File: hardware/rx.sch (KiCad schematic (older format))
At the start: 19 parts, among them P1 SMA, U11 SKY65404, U9 TRF37A73

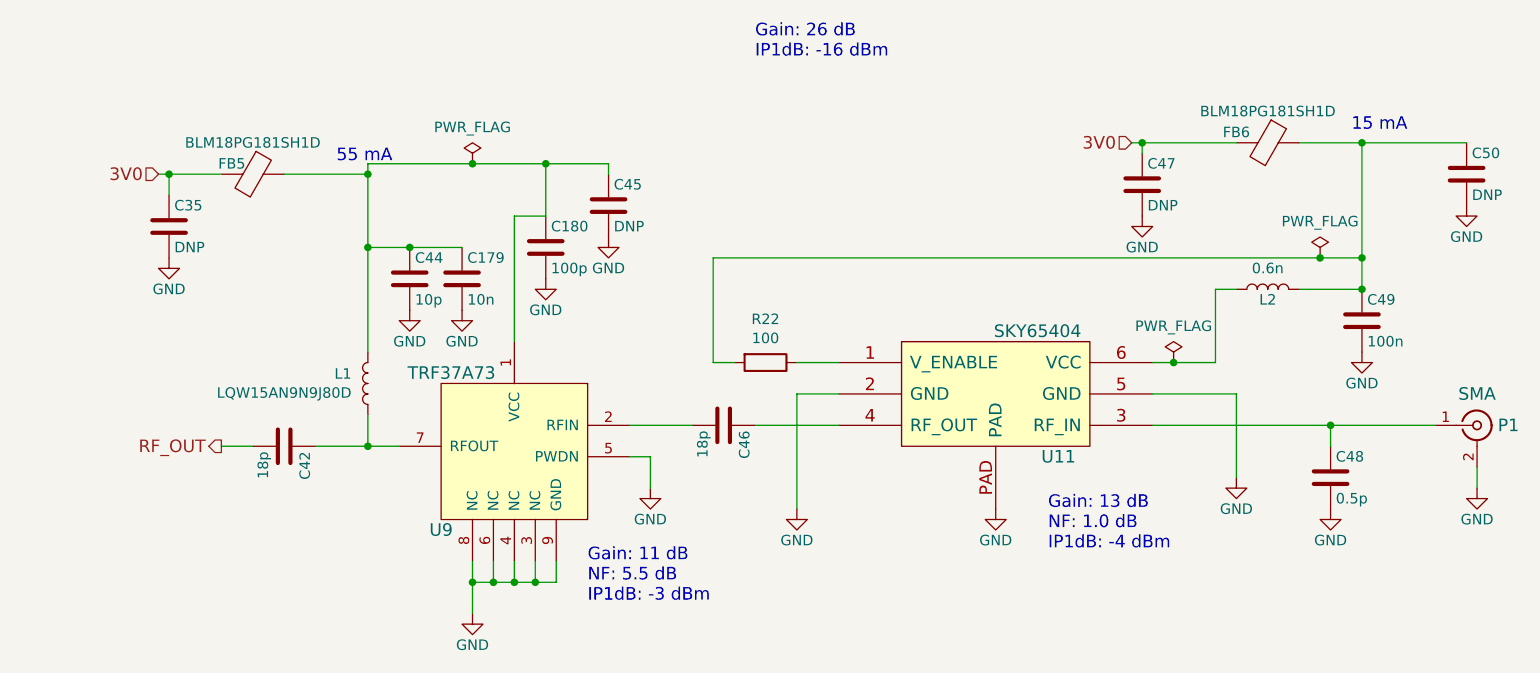
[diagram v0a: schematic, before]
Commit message: Improved tx sheet and corresponding documentation.
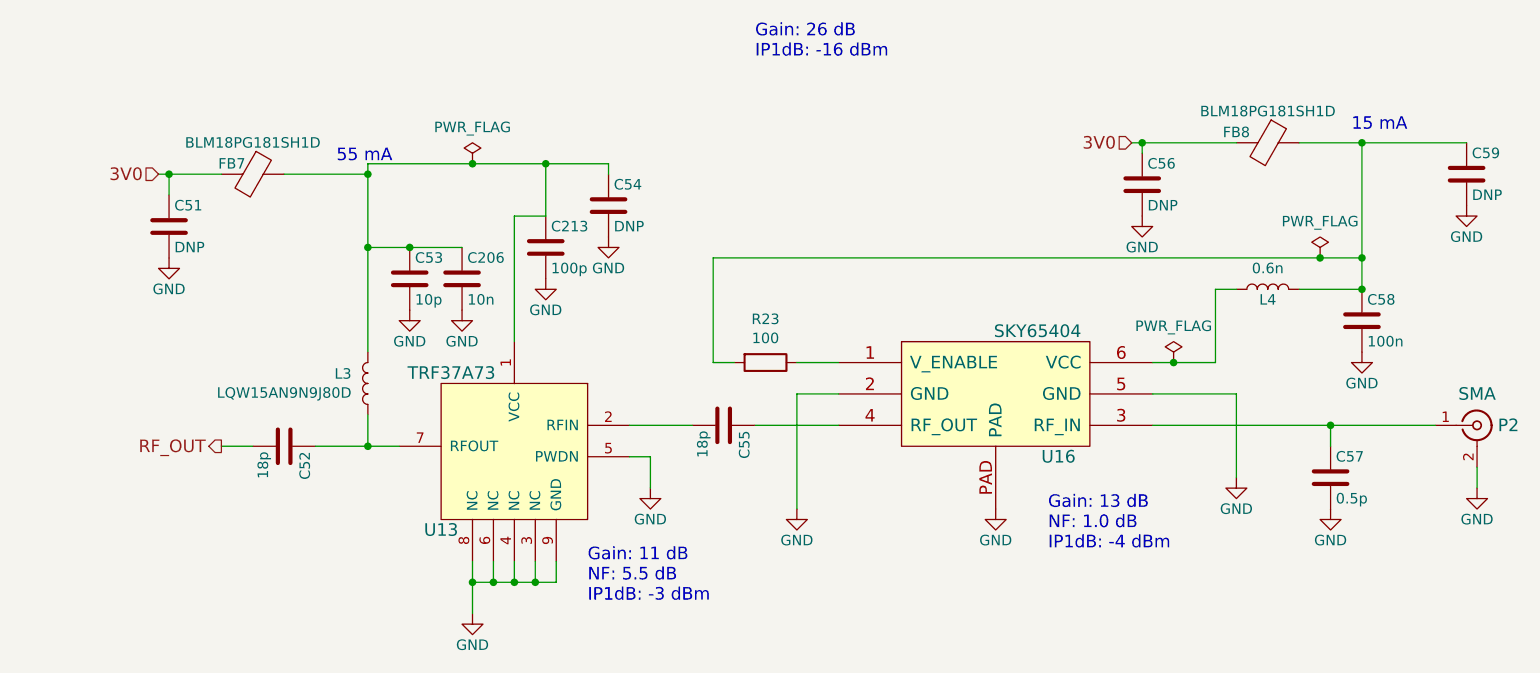
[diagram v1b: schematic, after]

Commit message: Improved documentation and parts of the schematic.
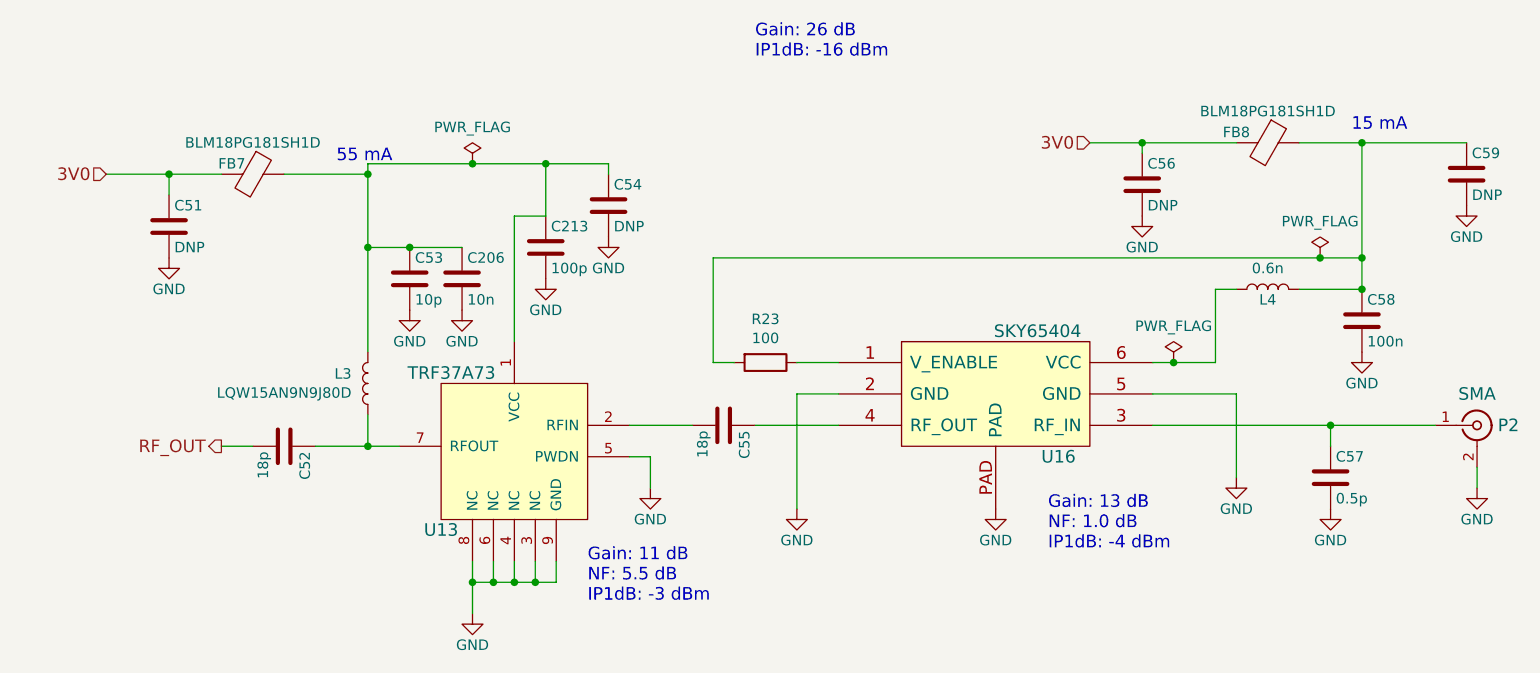
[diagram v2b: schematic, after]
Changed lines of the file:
@@
 $Descr A4 11693 8268
 encoding utf-8
-Sheet 6 10
+Sheet 7 10
 Title ""
 Date ""
@@
 Wire Wire Line
 	8600 2600 8600 3150
-Text HLabel 2850 2750 0    60   Input ~ 0
+Text HLabel 2600 2750 0    60   Input ~ 0
 3V0
-Text HLabel 7500 2600 0    60   Input ~ 0
+Text HLabel 7300 2600 0    60   Input ~ 0
 3V0
 Text HLabel 3150 4050 0    60   Output ~ 0
@@
 $EndComp
 Wire Wire Line
-	2850 2750 2900 2750
+	2600 2750 2900 2750
 $Comp
 L Device:C C54
@@
 $EndComp
 Wire Wire Line
-	7500 2600 7550 2600
+	7300 2600 7550 2600
 $Comp
 L Device:C C50

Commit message: Changed components to official libs.
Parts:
- added C51: 100n, Capacitor_SMD:C_0402_1005Metric, symbol Device:C
- C35, C47, C50: value DNP -> 100n; footprint Capacitor_SMD:C_0603_1608Metric -> Capacitor_SMD:C_0402_1005Metric; MFN (none) -> CL05B104KO5NNNC
- U11: footprint fmcw:XFDFN-6 -> Package_DFN_QFN:Skyworks_DFN-6-1EP_1.5x1.5mm_P0.5mm_EP0.7x1.2mm; symbol fmcw-rescue:SKY65404-fmcw3-rescue -> RF_Amplifier:SKY65404
- U9: footprint fmcw:DFN-8-1EP_2x2mm_Pitch0.5mm -> Package_SON:WSON-8-1EP_2x2mm_P0.5mm_EP0.9x1.6mm; symbol fmcw-rescue:TRF37A75-fmcw3-rescue -> RF_Amplifier:TRF37A73
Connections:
- net 3V0: now also C51.1; no longer C47.1
- net GND: now also U11.7 (EP), C51.2; no longer U11.PAD, U9.3 (NC), U9.4 (NC), U9.6 (NC), U9.8 (NC)
- net at C179.1, C180.1, C44.1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: now also C47.1
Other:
- moved on the sheet: C42, C48, C49, FB5, FB6, L1, L2, R22

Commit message: Finished design, began routing.
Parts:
- renumbered C35 to C145, C47 to C146, C42 to C147, C44 to C148, C179 to C149, C180 to C150, C46 to C152, C49 to C153, C48 to C154, C50 to C155, C51 to C156, C54 to C163, FB7 to FB13, FB8 to FB14, P1 to J4, R22 to R49, U9 to U22, U11 to U23

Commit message: Completed clock placement and routing.
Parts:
- removed C146, C155: 100n, Capacitor_SMD:C_0402_1005Metric, symbol Device:C

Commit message: Better MFNs for RF DC blocking caps.
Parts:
- C147, C152: MFN CL05C180GB5NCNC -> 500R07S180GV4T
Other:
- moved on the sheet: C163
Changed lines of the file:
@@
 $Descr A4 11693 8268
 encoding utf-8
-Sheet 6 10
+Sheet 7 10
 Title ""
 Date ""
@@
 F 2 "Capacitor_SMD:C_0402_1005Metric" H 5588 3800 30  0001 C CNN
 F 3 "" H 5550 3950 60  0000 C CNN
-F 4 "CL05C180GB5NCNC" H 0   0   50  0001 C CNN "MFN"
+F 4 "500R07S180GV4T" H 0   0   50  0001 C CNN "MFN"
 	1    5550 3950
 	0    1    1    0
@@
 F 2 "Capacitor_SMD:C_0402_1005Metric" H 3488 3800 30  0001 C CNN
 F 3 "" H 3450 3950 60  0000 C CNN
-F 4 "CL05C180GB5NCNC" H 0   -100 50  0001 C CNN "MFN"
+F 4 "500R07S180GV4T" H 0   -100 50  0001 C CNN "MFN"
 	1    3450 3950
 	0    1    1    0
@@
 L Device:C C163
 U 1 1 59751D28
-P 5000 2900
+P 5150 2900
 AR Path="/593D90BA/59751D28" Ref="C163"  Part="1"
 AR Path="/59396B97/59751D28" Ref="C151"  Part="1"
-F 0 "C163" H 5025 3000 50  0000 L CNN
-F 1 "DNP" H 5025 2800 50  0000 L CNN
-F 2 "Capacitor_SMD:C_0603_1608Metric" H 5038 2750 30  0001 C CNN
-F 3 "" H 5000 2900 60  0000 C CNN
-	1    5000 2900
+F 0 "C163" H 5175 3000 50  0000 L CNN
+F 1 "DNP" H 5175 2800 50  0000 L CNN
+F 2 "Capacitor_SMD:C_0603_1608Metric" H 5188 2750 30  0001 C CNN
+F 3 "" H 5150 2900 60  0000 C CNN
+	1    5150 2900
 	1    0    0    -1
 $EndComp
@@
 L power:GND #PWR0170
 U 1 1 59751D9B
-P 5000 3050
+P 5150 3100
 AR Path="/593D90BA/59751D9B" Ref="#PWR0170"  Part="1"
 AR Path="/59396B97/59751D9B" Ref="#PWR0156"  Part="1"
-F 0 "#PWR0170" H 5000 2800 50  0001 C CNN
-F 1 "GND" H 5000 2900 50  0000 C CNN
-F 2 "" H 5000 3050 60  0000 C CNN
-F 3 "" H 5000 3050 60  0000 C CNN
-	1    5000 3050
+F 0 "#PWR0170" H 5150 2850 50  0001 C CNN
+F 1 "GND" H 5150 2950 50  0000 C CNN
+F 2 "" H 5150 3100 60  0000 C CNN
+F 3 "" H 5150 3100 60  0000 C CNN
+	1    5150 3100
 	1    0    0    -1
 $EndComp
@@
 	4700 2950 4700 2700
 Connection ~ 4700 2700
-Wire Wire Line
-	5000 2750 5000 2700
 $Comp
 L Device:C C149
@@
 	1    0    0    -1
 $EndComp
-Wire Wire Line
-	5000 2700 4700 2700
 Text Notes 5700 2200 0    60   ~ 0
 Gain: 26 dB\nIP1dB: -16 dBm
@@
 Wire Wire Line
 	7200 2600 7550 2600
+Wire Wire Line
+	5150 2700 5150 2750
+Wire Wire Line
+	4700 2700 5150 2700
+Wire Wire Line
+	5150 3100 5150 3050
 $EndSCHEMATC

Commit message: Completed transmitter placement/routing.
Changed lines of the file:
@@
 $Descr A4 11693 8268
 encoding utf-8
-Sheet 7 10
+Sheet 6 10
 Title ""
 Date ""
@@
 AR Path="/59396B97/593BC199" Ref="U23"  Part="1"
 AR Path="/593D90BA/593BC199" Ref="U25"  Part="1"
-F 0 "U25" H 6550 4150 60  0000 R CNN
+F 0 "U23" H 6550 4150 60  0000 R CNN
 F 1 "SKY65404" H 6550 4050 60  0000 R CNN
 F 2 "Package_DFN_QFN:Skyworks_DFN-6-1EP_1.5x1.5mm_P0.5mm_EP0.7x1.2mm" H 6750 3950 60  0001 C CNN
@@
 AR Path="/59396B97/593BC25F" Ref="#PWR0158"  Part="1"
 AR Path="/593D90BA/593BC25F" Ref="#PWR0172"  Part="1"
-F 0 "#PWR0172" H 6800 4000 50  0001 C CNN
+F 0 "#PWR0158" H 6800 4000 50  0001 C CNN
 F 1 "GND" H 6800 4100 50  0000 C CNN
 F 2 "" H 6800 4250 60  0000 C CNN
@@
 AR Path="/59396B97/593BC396" Ref="R49"  Part="1"
 AR Path="/593D90BA/593BC396" Ref="R50"  Part="1"
-F 0 "R50" H 6730 3354 50  0000 R CNN
+F 0 "R49" H 6730 3354 50  0000 R CNN
 F 1 "100" H 6730 3445 50  0000 R CNN
 F 2 "Resistor_SMD:R_0402_1005Metric" V 6730 3400 30  0001 C CNN
@@
 AR Path="/59396B97/593BC695" Ref="L2"  Part="1"
 AR Path="/593D90BA/593BC695" Ref="L4"  Part="1"
-F 0 "L4" H 6753 3354 50  0000 L CNN
+F 0 "L2" H 6753 3354 50  0000 L CNN
 F 1 "0.6n" H 6753 3445 50  0000 L CNN
 F 2 "Inductor_SMD:L_0402_1005Metric" H 6700 3400 60  0001 C CNN
@@
 AR Path="/59396B97/593BC767" Ref="C153"  Part="1"
 AR Path="/593D90BA/593BC767" Ref="C165"  Part="1"
-F 0 "C165" H 6135 3446 50  0000 R CNN
+F 0 "C153" H 6135 3446 50  0000 R CNN
 F 1 "100n" H 6135 3355 50  0000 R CNN
 F 2 "Capacitor_SMD:C_0402_1005Metric" H 6288 3250 30  0001 C CNN
@@
 AR Path="/59396B97/593BC7DB" Ref="#PWR0157"  Part="1"
 AR Path="/593D90BA/593BC7DB" Ref="#PWR0171"  Part="1"
-F 0 "#PWR0171" H 6250 3350 50  0001 C CNN
+F 0 "#PWR0157" H 6250 3350 50  0001 C CNN
 F 1 "GND" H 6250 3450 50  0000 C CNN
 F 2 "" H 6250 3600 60  0000 C CNN
@@
 AR Path="/59396B97/593BCCCA" Ref="J4"  Part="1"
 AR Path="/593D90BA/593BCCCA" Ref="J5"  Part="1"
-F 0 "J5" H 9300 3950 60  0000 C CNN
+F 0 "J4" H 9300 3950 60  0000 C CNN
 F 1 "SMA" H 9150 4100 60  0000 C CNN
 F 2 "fmcw:CONSMA003.062" H 9150 3950 60  0001 C CNN
@@
 AR Path="/59396B97/593BCD59" Ref="#PWR0162"  Part="1"
 AR Path="/593D90BA/593BCD59" Ref="#PWR0176"  Part="1"
-F 0 "#PWR0176" H 9150 4000 50  0001 C CNN
+F 0 "#PWR0162" H 9150 4000 50  0001 C CNN
 F 1 "GND" H 9150 4100 50  0000 C CNN
 F 2 "" H 9150 4250 60  0000 C CNN
@@
 AR Path="/59396B97/593BCEBC" Ref="C154"  Part="1"
 AR Path="/593D90BA/593BCEBC" Ref="C166"  Part="1"
-F 0 "C166" H 7225 4300 50  0000 L CNN
+F 0 "C154" H 7225 4300 50  0000 L CNN
 F 1 "0.5p" H 7225 4100 50  0000 L CNN
 F 2 "Capacitor_SMD:C_0402_1005Metric" H 7238 4050 30  0001 C CNN
@@
 AR Path="/59396B97/593BCF37" Ref="#PWR0159"  Part="1"
 AR Path="/593D90BA/593BCF37" Ref="#PWR0173"  Part="1"
-F 0 "#PWR0173" H 7200 4100 50  0001 C CNN
+F 0 "#PWR0159" H 7200 4100 50  0001 C CNN
 F 1 "GND" H 7200 4200 50  0000 C CNN
 F 2 "" H 7200 4350 60  0000 C CNN
@@
 AR Path="/59396B97/593BD4EF" Ref="C152"  Part="1"
 AR Path="/593D90BA/593BD4EF" Ref="C164"  Part="1"
-F 0 "C164" V 5298 3950 50  0000 C CNN
+F 0 "C152" V 5298 3950 50  0000 C CNN
 F 1 "18p" V 5389 3950 50  0000 C CNN
 F 2 "Capacitor_SMD:C_0402_1005Metric" H 5588 3800 30  0001 C CNN
@@
 AR Path="/59396B97/593BD727" Ref="#PWR0153"  Part="1"
 AR Path="/593D90BA/593BD727" Ref="#PWR0167"  Part="1"
-F 0 "#PWR0167" H 4550 3950 50  0001 C CNN
+F 0 "#PWR0153" H 4550 3950 50  0001 C CNN
 F 1 "GND" H 4550 4050 50  0000 C CNN
 F 2 "" H 4550 4200 60  0000 C CNN
@@
 AR Path="/59396B97/593BD8E8" Ref="L1"  Part="1"
 AR Path="/593D90BA/593BD8E8" Ref="L3"  Part="1"
-F 0 "L3" H 3928 3454 50  0000 L CNN
+F 0 "L1" H 3928 3454 50  0000 L CNN
 F 1 "LQW15AN9N9J80D" H 3928 3545 50  0000 L CNN
 F 2 "Inductor_SMD:L_0402_1005Metric" H 3850 3500 60  0001 C CNN
@@
 AR Path="/59396B97/593BDA25" Ref="C148"  Part="1"
 AR Path="/593D90BA/593BDA25" Ref="C160"  Part="1"
-F 0 "C160" H 4075 3350 50  0000 L CNN
+F 0 "C148" H 4075 3350 50  0000 L CNN
 F 1 "10p" H 4075 3150 50  0000 L CNN
 F 2 "Capacitor_SMD:C_0402_1005Metric" H 4088 3100 30  0001 C CNN
@@
 AR Path="/59396B97/593BDABD" Ref="#PWR0151"  Part="1"
 AR Path="/593D90BA/593BDABD" Ref="#PWR0165"  Part="1"
-F 0 "#PWR0165" H 4050 3150 50  0001 C CNN
+F 0 "#PWR0151" H 4050 3150 50  0001 C CNN
 F 1 "GND" H 4050 3250 50  0000 C CNN
 F 2 "" H 4050 3400 60  0000 C CNN
@@
 AR Path="/59396B97/593BDF98" Ref="C147"  Part="1"
 AR Path="/593D90BA/593BDF98" Ref="C159"  Part="1"
-F 0 "C159" V 3198 3950 50  0000 C CNN
+F 0 "C147" V 3198 3950 50  0000 C CNN
 F 1 "18p" V 3289 3950 50  0000 C CNN
 F 2 "Capacitor_SMD:C_0402_1005Metric" H 3488 3800 30  0001 C CNN
@@
 AR Path="/593D90BA/59751767" Ref="FB13"  Part="1"
 AR Path="/59396B97/59751767" Ref="FB11"  Part="1"
-F 0 "FB13" V 2876 2700 50  0000 C CNN
+F 0 "FB11" V 2876 2700 50  0000 C CNN
 F 1 "BLM18PG181SH1D" V 2967 2700 50  0000 C CNN
 F 2 "Inductor_SMD:L_0603_1608Metric" H 3150 2700 60  0001 C CNN
@@
 AR Path="/593D90BA/59751D28" Ref="C163"  Part="1"
 AR Path="/59396B97/59751D28" Ref="C151"  Part="1"
-F 0 "C163" H 5175 3000 50  0000 L CNN
+F 0 "C151" H 5175 3000 50  0000 L CNN
 F 1 "DNP" H 5175 2800 50  0000 L CNN
 F 2 "Capacitor_SMD:C_0603_1608Metric" H 5188 2750 30  0001 C CNN
@@
 AR Path="/593D90BA/59751D9B" Ref="#PWR0170"  Part="1"
 AR Path="/59396B97/59751D9B" Ref="#PWR0156"  Part="1"
-F 0 "#PWR0170" H 5150 2850 50  0001 C CNN
+F 0 "#PWR0156" H 5150 2850 50  0001 C CNN
 F 1 "GND" H 5150 2950 50  0000 C CNN
 F 2 "" H 5150 3100 60  0000 C CNN
@@
 AR Path="/593D90BA/597527FA" Ref="FB14"  Part="1"
 AR Path="/59396B97/597527FA" Ref="FB12"  Part="1"
-F 0 "FB14" V 7426 2600 50  0000 C CNN
+F 0 "FB12" V 7426 2600 50  0000 C CNN
 F 1 "BLM18PG181SH1D" V 7517 2600 50  0000 C CNN
 F 2 "Inductor_SMD:L_0603_1608Metric" H 7700 2600 60  0001 C CNN
@@
 AR Path="/59396B97/59752CE4" Ref="#PWR0161"  Part="1"
 AR Path="/593D90BA/59752CE4" Ref="#PWR0175"  Part="1"
-F 0 "#PWR0175" H 8050 2750 50  0001 C CNN
+F 0 "#PWR0161" H 8050 2750 50  0001 C CNN
 F 1 "GND" H 8050 2850 50  0000 C CNN
 F 2 "" H 8050 3000 60  0000 C CNN
@@
 AR Path="/593D90BA/597605DF" Ref="U24"  Part="1"
 AR Path="/597605DF" Ref="U?"  Part="1"
-F 0 "U24" H 4409 4003 60  0000 R CNN
+F 0 "U22" H 4409 4003 60  0000 R CNN
 F 1 "TRF37A73" H 4409 3897 60  0000 R CNN
 F 2 "Package_SON:WSON-8-1EP_2x2mm_P0.5mm_EP0.9x1.6mm" H 4450 3900 60  0001 C CNN
@@
 AR Path="/59396B97/59761DBE" Ref="C150"  Part="1"
 AR Path="/593D90BA/59761DBE" Ref="C162"  Part="1"
-F 0 "C162" H 4725 3200 50  0000 L CNN
+F 0 "C150" H 4725 3200 50  0000 L CNN
 F 1 "100p" H 4725 3000 50  0000 L CNN
 F 2 "Capacitor_SMD:C_0402_1005Metric" H 4738 2950 30  0001 C CNN
@@
 AR Path="/59396B97/59761E7D" Ref="#PWR0154"  Part="1"
 AR Path="/593D90BA/59761E7D" Ref="#PWR0168"  Part="1"
-F 0 "#PWR0168" H 4700 3000 50  0001 C CNN
+F 0 "#PWR0154" H 4700 3000 50  0001 C CNN
 F 1 "GND" H 4700 3100 50  0000 C CNN
 F 2 "" H 4700 3250 60  0000 C CNN
@@
 AR Path="/59396B97/59762FC5" Ref="C149"  Part="1"
 AR Path="/593D90BA/59762FC5" Ref="C161"  Part="1"
-F 0 "C161" H 4325 3350 50  0000 L CNN
+F 0 "C149" H 4325 3350 50  0000 L CNN
 F 1 "10n" H 4325 3150 50  0000 L CNN
 F 2 "Capacitor_SMD:C_0402_1005Metric" H 4338 3100 30  0001 C CNN
@@
 AR Path="/59396B97/5976305E" Ref="#PWR0152"  Part="1"
 AR Path="/593D90BA/5976305E" Ref="#PWR0166"  Part="1"
-F 0 "#PWR0166" H 4300 3150 50  0001 C CNN
+F 0 "#PWR0152" H 4300 3150 50  0001 C CNN
 F 1 "GND" H 4300 3250 50  0000 C CNN
 F 2 "" H 4300 3400 60  0000 C CNN
@@
 AR Path="/59396B97/5CF2FC64" Ref="#FLG011"  Part="1"
 AR Path="/593D90BA/5CF2FC64" Ref="#FLG014"  Part="1"
-F 0 "#FLG014" H 4350 2775 50  0001 C CNN
+F 0 "#FLG011" H 4350 2775 50  0001 C CNN
 F 1 "PWR_FLAG" H 4350 2874 50  0000 C CNN
 F 2 "" H 4350 2700 50  0001 C CNN
@@
 AR Path="/59396B97/5CF2FCC1" Ref="#FLG013"  Part="1"
 AR Path="/593D90BA/5CF2FCC1" Ref="#FLG016"  Part="1"
-F 0 "#FLG016" H 6950 3225 50  0001 C CNN
+F 0 "#FLG013" H 6950 3225 50  0001 C CNN
 F 1 "PWR_FLAG" H 6950 3324 50  0000 C CNN
 F 2 "" H 6950 3150 50  0001 C CNN
@@
 AR Path="/59396B97/5CF3D956" Ref="#FLG012"  Part="1"
 AR Path="/593D90BA/5CF3D956" Ref="#FLG015"  Part="1"
-F 0 "#FLG015" H 6700 3725 50  0001 C CNN
+F 0 "#FLG012" H 6700 3725 50  0001 C CNN
 F 1 "PWR_FLAG" V 6800 3700 50  0000 L CNN
 F 2 "" H 6700 3650 50  0001 C CNN
@@
 AR Path="/59396B97/5C429467" Ref="#PWR0155"  Part="1"
 AR Path="/593D90BA/5C429467" Ref="#PWR0169"  Part="1"
-F 0 "#PWR0169" H 4900 3350 50  0001 C CNN
+F 0 "#PWR0155" H 4900 3350 50  0001 C CNN
 F 1 "GND" H 4900 3450 50  0000 C CNN
 F 2 "" H 4900 3600 60  0000 C CNN
@@
 AR Path="/59396B97/5C42C3BD" Ref="C156"  Part="1"
 AR Path="/593D90BA/5C42C3BD" Ref="C168"  Part="1"
-F 0 "C168" H 8165 2846 50  0000 L CNN
+F 0 "C156" H 8165 2846 50  0000 L CNN
 F 1 "100n" H 8165 2755 50  0000 L CNN
 F 2 "Capacitor_SMD:C_0402_1005Metric" H 8088 2650 30  0001 C CNN
@@
 AR Path="/59396B97/5C42DC20" Ref="C145"  Part="1"
 AR Path="/593D90BA/5C42DC20" Ref="C157"  Part="1"
-F 0 "C157" H 2865 2946 50  0000 L CNN
+F 0 "C145" H 2865 2946 50  0000 L CNN
 F 1 "100n" H 2865 2855 50  0000 L CNN
 F 2 "Capacitor_SMD:C_0402_1005Metric" H 2788 2750 30  0001 C CNN
@@
 AR Path="/59396B97/5C430750" Ref="#PWR0149"  Part="1"
 AR Path="/593D90BA/5C430750" Ref="#PWR0163"  Part="1"
-F 0 "#PWR0163" H 2750 2850 50  0001 C CNN
+F 0 "#PWR0149" H 2750 2850 50  0001 C CNN
 F 1 "GND" H 2755 2927 50  0000 C CNN
 F 2 "" H 2750 3100 50  0001 C CNN
